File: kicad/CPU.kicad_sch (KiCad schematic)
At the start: 40 parts, among them J1 Conn_ARM_SWD_TagConnect_TC203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, J2 Screw_Terminal_01x03, J3 Screw_Terminal_01x03, SW1 SW_Push, U7 STM32F303CBTx, Y1 8 MHz

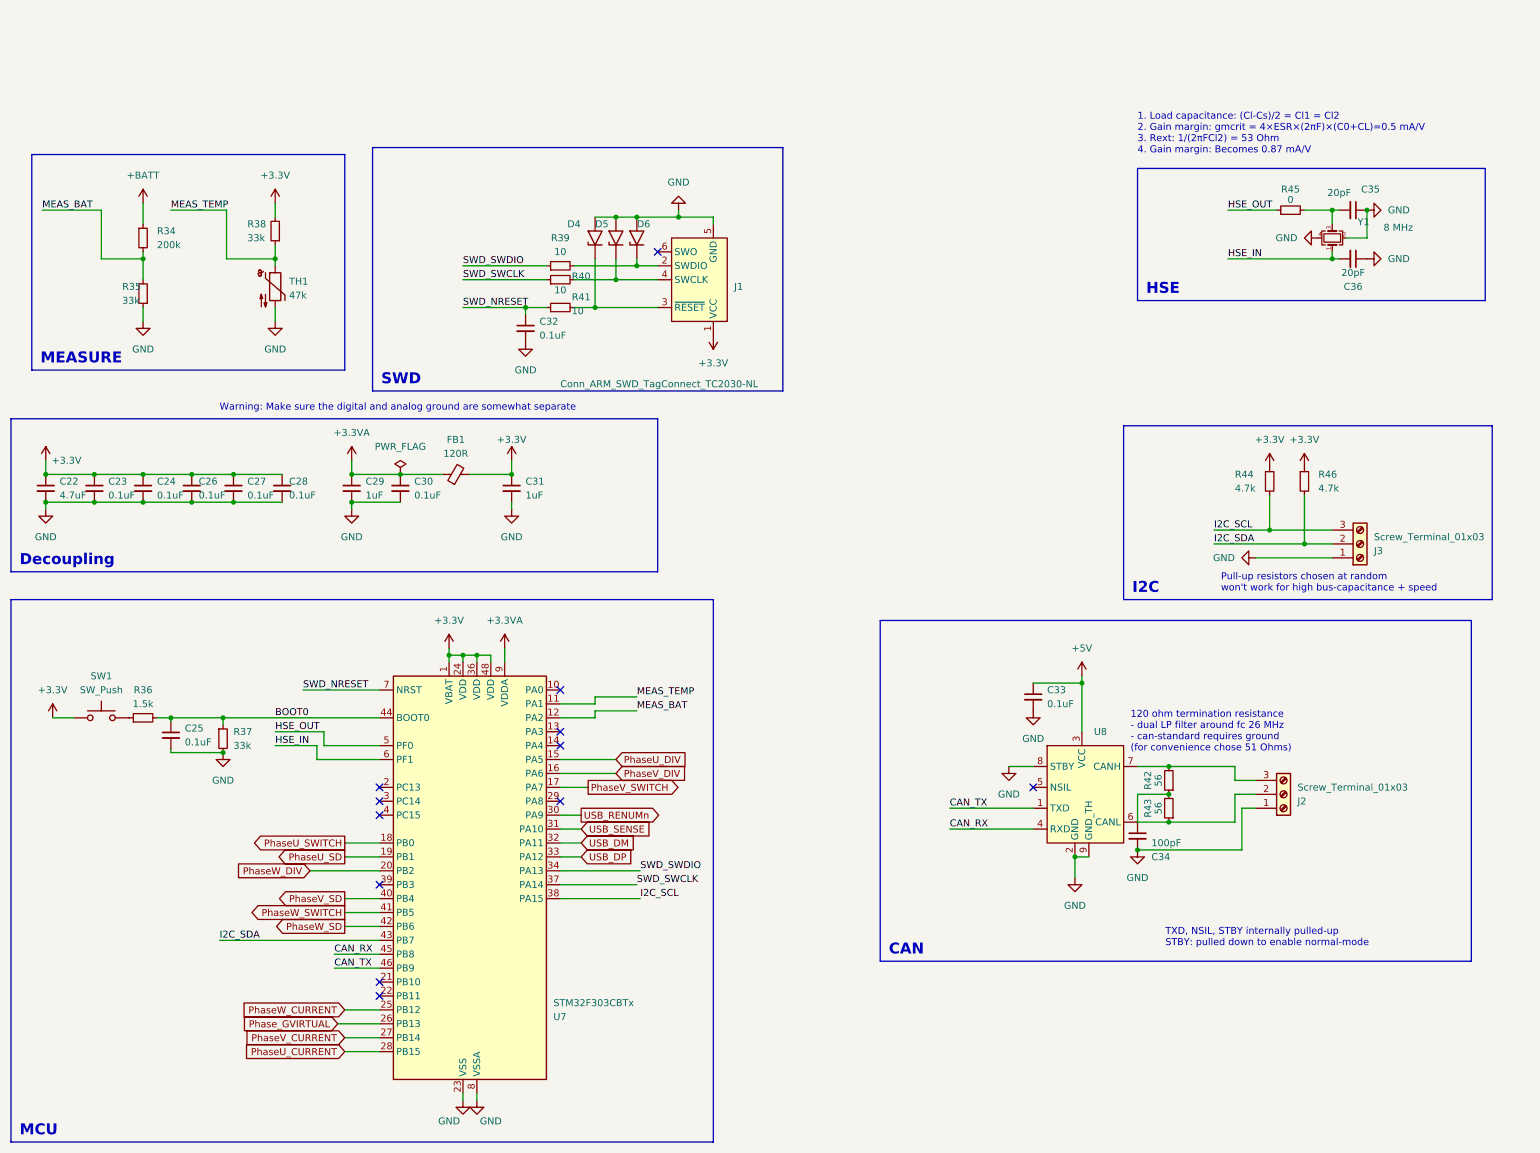
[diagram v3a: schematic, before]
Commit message: [kicad] Removed ESD diodes for SWD, changed SWD resistor to smaller size
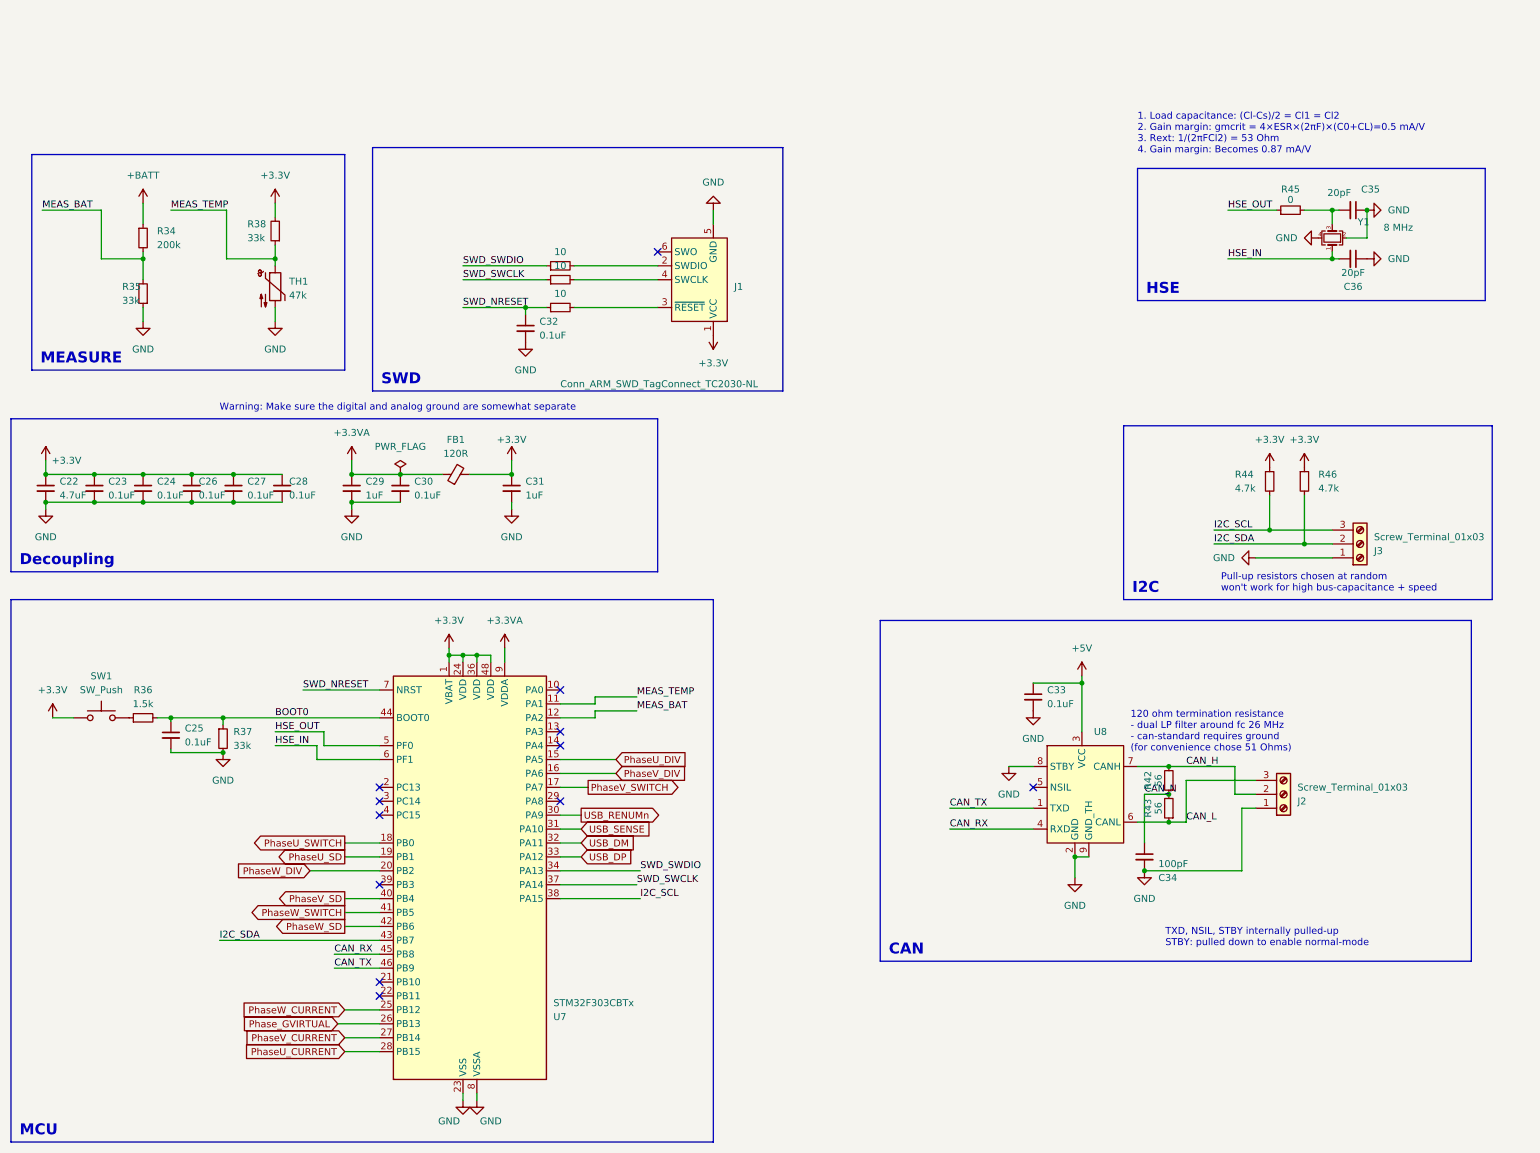
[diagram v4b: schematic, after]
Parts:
- removed D4, D5, D6: SMAJ6.5CA, Diode_SMD:D_SMA, symbol Diode:SMAJ13A
- R39, R40, R41: footprint Resistor_SMD:R_1206_3216Metric -> Resistor_SMD:R_0402_1005Metric; MFR.Part 1206W4F100JT5E -> 0402WGF100JTCE; jlcpcb C17903 -> C25077
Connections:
- net CAN_N: now reaches C34.1, R42.1, R43.2
- net CAN_N: no longer J2.2 (Pin_2), R43.1, U8.6 (CANL)
- net CAN_H: now reaches R42.2, U8.7 (CANH)
- net CAN_H: now also J2.2 (Pin_2); no longer J2.3 (Pin_3)
- new net CAN_L: J2.3 (Pin_3), R43.1, U8.6 (CANL)
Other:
- moved on the sheet: C34

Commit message: [kicad] Experimented with component placing
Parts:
- SW1: MFR.Part 5.8 ZSGT -> SPEH110100; jlcpcb C2681587 -> C97448
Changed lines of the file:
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@@
       (effects (font (size 1.27 1.27)) hide)
     )
-    (property "jlcpcb" "C2681587" (at 30.48 118.11 0)
+    (property "jlcpcb" "C97448" (at 30.48 118.11 0)
       (effects (font (size 1.27 1.27)) hide)
     )
-    (property "MFR.Part" "5.8 ZSGT" (at 30.48 118.11 0)
+    (property "MFR.Part" "SPEH110100" (at 30.48 118.11 0)
       (effects (font (size 1.27 1.27)) hide)
     )

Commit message: [kicad] Layout, mostly power traces + HS signal traces
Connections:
- net USB_DM renamed USB_DN
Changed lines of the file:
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@@
     )
   )
-  (global_label "USB_DM" (shape input) (at 118.11 140.97 0) (fields_autoplaced)
+  (global_label "USB_DN" (shape input) (at 118.11 140.97 0) (fields_autoplaced)
     (effects (font (size 1.27 1.27)) (justify left))
-    (property "Intersheetrefs" "${INTERSHEET_REFS}" (at 128.5942 140.97 0)
+    (property "Intersheetrefs" "${INTERSHEET_REFS}" (at 128.4733 140.97 0)
       (effects (font (size 1.27 1.27)) (justify left) hide)
     )

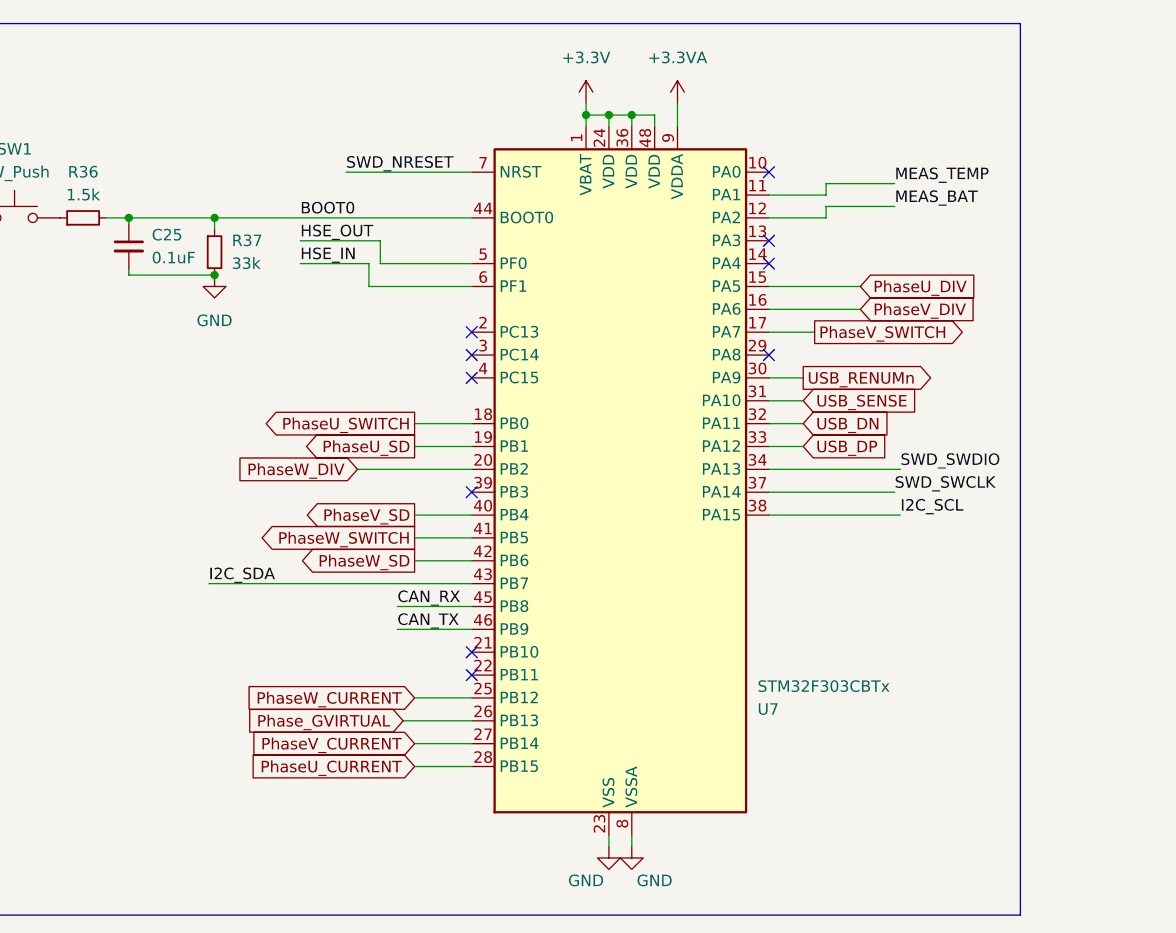
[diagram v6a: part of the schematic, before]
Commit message: [kicad] Changed CPU adc / pwm inputs to facilitate routing
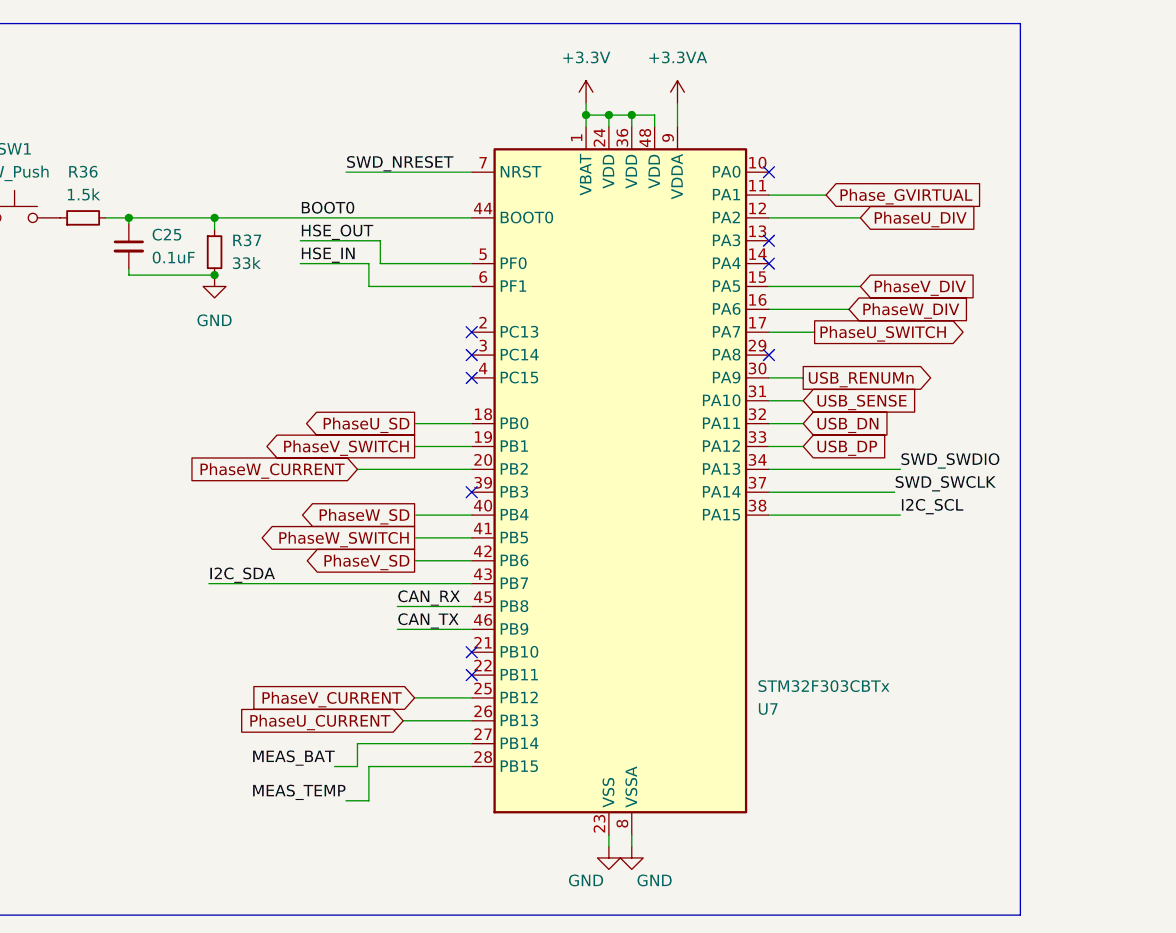
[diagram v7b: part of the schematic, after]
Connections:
- net MEAS_BAT: now also U7.27 (PB14); no longer U7.12 (PA2)
- net MEAS_TEMP: now also U7.28 (PB15); no longer U7.11 (PA1)
- net PhaseU_CURRENT: now also U7.26 (PB13); no longer U7.28 (PB15)
- net PhaseU_DIV: now also U7.12 (PA2); no longer U7.15 (PA5)
- net PhaseU_SD: now also U7.18 (PB0); no longer U7.19 (PB1)
- net PhaseU_SWITCH: now also U7.17 (PA7); no longer U7.18 (PB0)
- net PhaseV_CURRENT: now also U7.25 (PB12); no longer U7.27 (PB14)
- net PhaseV_DIV: now also U7.15 (PA5); no longer U7.16 (PA6)
- net PhaseV_SD: now also U7.42 (PB6); no longer U7.40 (PB4)
- net PhaseV_SWITCH: now also U7.19 (PB1); no longer U7.17 (PA7)
- net PhaseW_CURRENT: now also U7.20 (PB2); no longer U7.25 (PB12)
- net PhaseW_DIV: now also U7.16 (PA6); no longer U7.20 (PB2)
- net PhaseW_SD: now also U7.40 (PB4); no longer U7.42 (PB6)
- net Phase_GVIRTUAL: now also U7.11 (PA1); no longer U7.26 (PB13)

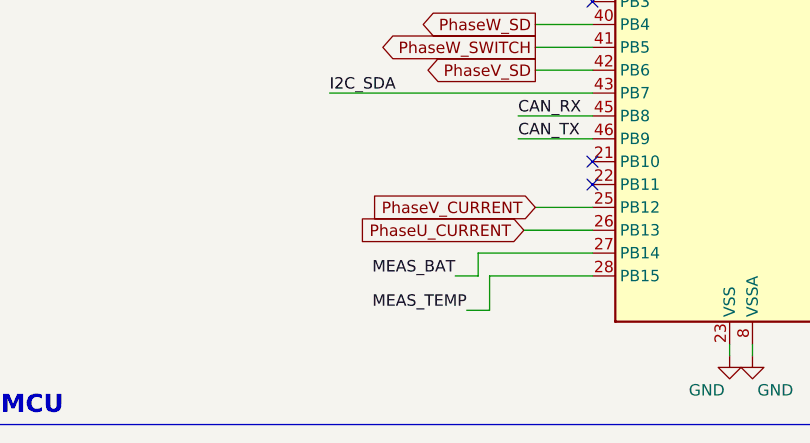
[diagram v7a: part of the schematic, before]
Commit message: Rough routing finished, checks next
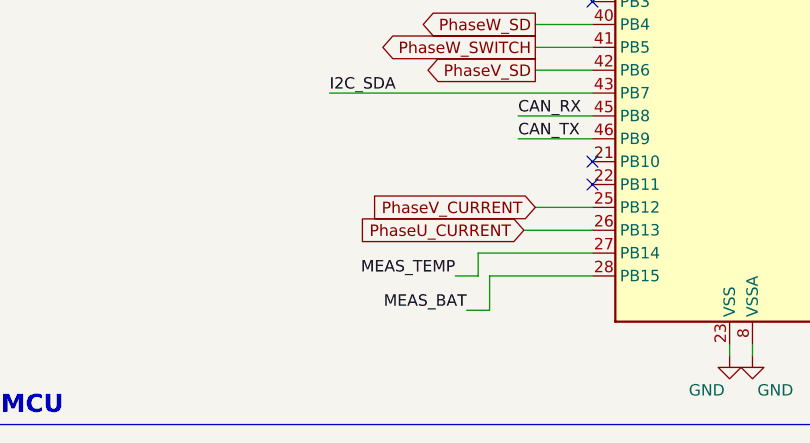
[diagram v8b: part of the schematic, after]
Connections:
- net MEAS_BAT: now also U7.28 (PB15); no longer U7.27 (PB14)
- net MEAS_TEMP: now also U7.27 (PB14); no longer U7.28 (PB15)
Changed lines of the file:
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@@
     (effects (font (size 1.27 1.27)) (justify left bottom))
   )
-  (label "MEAS_BAT" (at 66.04 179.07 180) (fields_autoplaced)
+  (label "MEAS_TEMP" (at 66.04 179.07 180) (fields_autoplaced)
     (effects (font (size 1.27 1.27)) (justify right bottom))
   )
@@
     (effects (font (size 1.27 1.27)) (justify left bottom))
   )
-  (label "MEAS_TEMP" (at 67.31 182.88 180) (fields_autoplaced)
+  (label "MEAS_BAT" (at 67.31 182.88 180) (fields_autoplaced)
     (effects (font (size 1.27 1.27)) (justify right bottom))
   )
